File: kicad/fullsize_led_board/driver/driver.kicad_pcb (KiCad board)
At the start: 2 copper layers, 163.5 x 127.5 mm, 131 parts, among them J4 Anodes Header, J5 Cathodes Header, Q1 SQ2351CES, Q10 SQ2351CES, Q11 SQ2351CES, Q12 SQ2351CES, Q13 SQ2351CES, Q14 SQ2351CES, Q15 SQ2351CES, Q16 SQ2351CES, Q17 SQ2351CES, Q18 SQ2351CES, Q19 SQ2351CES, Q2 SQ2351CES, Q20 SQ2351CES, Q21 SQ2351CES, Q22 SQ2351CES, Q23 SQ2351CES, Q24 SQ2351CES, Q3 SQ2351CES, Q4 SQ2351CES, Q5 SQ2351CES, Q6 SQ2351CES, Q7 SQ2351CES, Q8 SQ2351CES, Q9 SQ2351CES, U1 74HCT541, U2 74HCT595, U3 74HCT595, U4 74HCT595, U5 TPIC6B595N, U6 TPIC6B595N, U7 TPIC6B595N, U8 TPIC6B595N

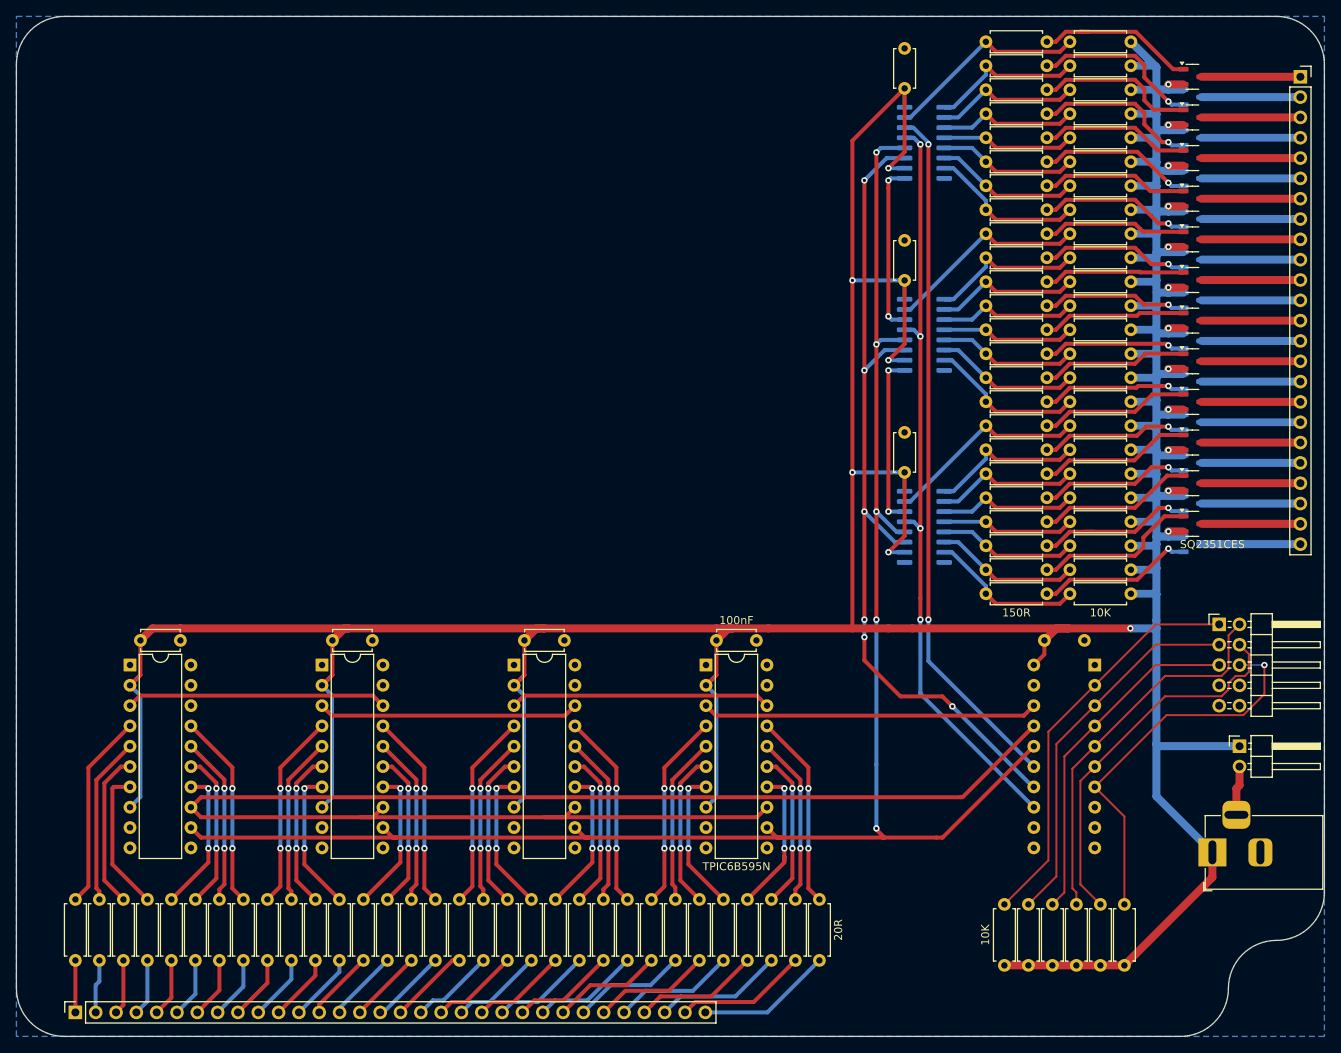
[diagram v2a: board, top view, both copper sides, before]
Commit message: fullsize led board: fixed backwards wiring
It's not as beautiful as I'd like to have it, but this will suffice, otherwise it will take way too much time to reroute the VIAs.
If I want to improve this design further, I'd like to use SMD resistors anyway, so a full rerout would be necessary.
Lesson learned I guess...
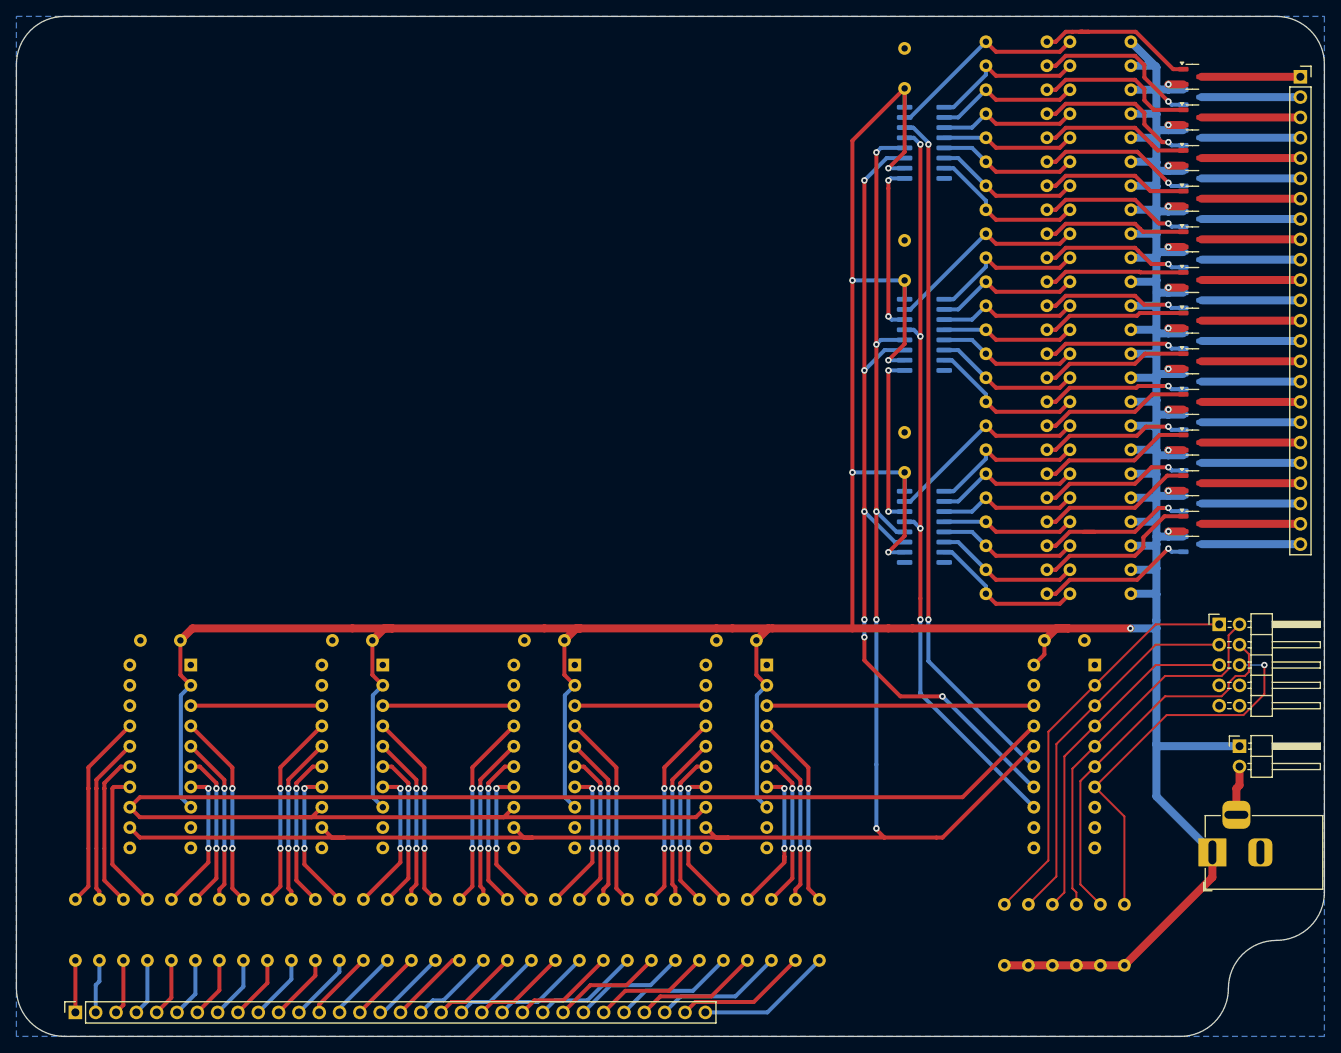
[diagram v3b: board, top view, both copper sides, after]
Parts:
- C2, C3, C4, C5, C6, C7, C8, R1, R10, R11, R12, R13, R14, R15, R16, R17, R18, R19, R2, R20, R21, R22, R23, R24, R25, R26, R27, R28, R29, R3, R30, R31, R32, R33, R34, R35, R36, R37, R38, R39, R4, R40, R41, R42, R43, R44, R45, R46, R47, R48, R49, R5, R50, R51, R52, R53, R54, R55, R56, R57, R58, R59, R6, R60, R61, R62, R63, R64, R65, R66, R67, R68, R69, R7, R70, R71, R72, R73, R74, R75, R76, R77, R78, R79, R8, R80, R81, R82, R83, R84, R85, R86, R9, U5, U6, U7, U8: moved to B.Cu
- moved R2 7.62 mm to (232.0, 143.5), turned to -90 degrees
- moved U6 7.60 mm to (142.3, 113.6), turned to 180 degrees
- moved U7 7.60 mm to (166.3, 113.6), turned to 180 degrees
- moved U8 7.60 mm to (190.3, 113.6), turned to 180 degrees
- moved U5 7.60 mm to (118.3, 113.6), turned to 180 degrees
- moved C5 5.00 mm to (117.0, 110.5), turned to 180 degrees
- moved C6 5.00 mm to (141.0, 110.5), turned to 180 degrees
- moved C7 5.00 mm to (165.0, 110.5), turned to 180 degrees
- moved C8 5.00 mm to (189.0, 110.5), turned to 180 degrees
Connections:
- R2 pad 1: +5V -> ShiftRowStrobe
- R2 pad 2: ShiftRowStrobe -> +5V
- U5 pad 14: /Cathodes4 -> /Cathodes3
- U5 pad 15: /Cathodes5 -> /Cathodes2
- U5 pad 16: /Cathodes6 -> /Cathodes1
- U5 pad 17: /Cathodes7 -> /Cathodes0
- U5 pad 4: /Cathodes0 -> /Cathodes7
- U5 pad 5: /Cathodes1 -> /Cathodes6
- U5 pad 6: /Cathodes2 -> /Cathodes5
- U5 pad 7: /Cathodes3 -> /Cathodes4
- U6 pad 14: /Cathodes12 -> /Cathodes11
- U6 pad 15: /Cathodes13 -> /Cathodes10
- U6 pad 16: /Cathodes14 -> /Cathodes9
- U6 pad 17: /Cathodes15 -> /Cathodes8
- U6 pad 4: /Cathodes8 -> /Cathodes15
- U6 pad 5: /Cathodes9 -> /Cathodes14
- U6 pad 6: /Cathodes10 -> /Cathodes13
- U6 pad 7: /Cathodes11 -> /Cathodes12
- U7 pad 14: /Cathodes20 -> /Cathodes19
- U7 pad 15: /Cathodes21 -> /Cathodes18
- U7 pad 16: /Cathodes22 -> /Cathodes17
- U7 pad 17: /Cathodes23 -> /Cathodes16
- U7 pad 4: /Cathodes16 -> /Cathodes23
- U7 pad 5: /Cathodes17 -> /Cathodes22
- U7 pad 6: /Cathodes18 -> /Cathodes21
- U7 pad 7: /Cathodes19 -> /Cathodes20
- U8 pad 14: /Cathodes28 -> /Cathodes27
- U8 pad 15: /Cathodes29 -> /Cathodes26
- U8 pad 16: /Cathodes30 -> /Cathodes25
- U8 pad 17: /Cathodes31 -> /Cathodes24
- U8 pad 4: /Cathodes24 -> /Cathodes31
- U8 pad 5: /Cathodes25 -> /Cathodes30
- U8 pad 6: /Cathodes26 -> /Cathodes29
- U8 pad 7: /Cathodes27 -> /Cathodes28
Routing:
- net Net-(U7-SER_IN): track 32.7 -> 16.4 mm
- net Net-(U6-SER_IN): track 32.7 -> 16.4 mm
- net Net-(U5-SER_IN): track 32.7 -> 16.4 mm
- net +5V: track 662.2 -> 649.3 mm
- net /ApplyRowAndStrobe': track 215.8 -> 225.9 mm
- net /RowData': track 42.0 -> 33.4 mm
- net /ShiftRowData': track 190.3 -> 198.1 mm

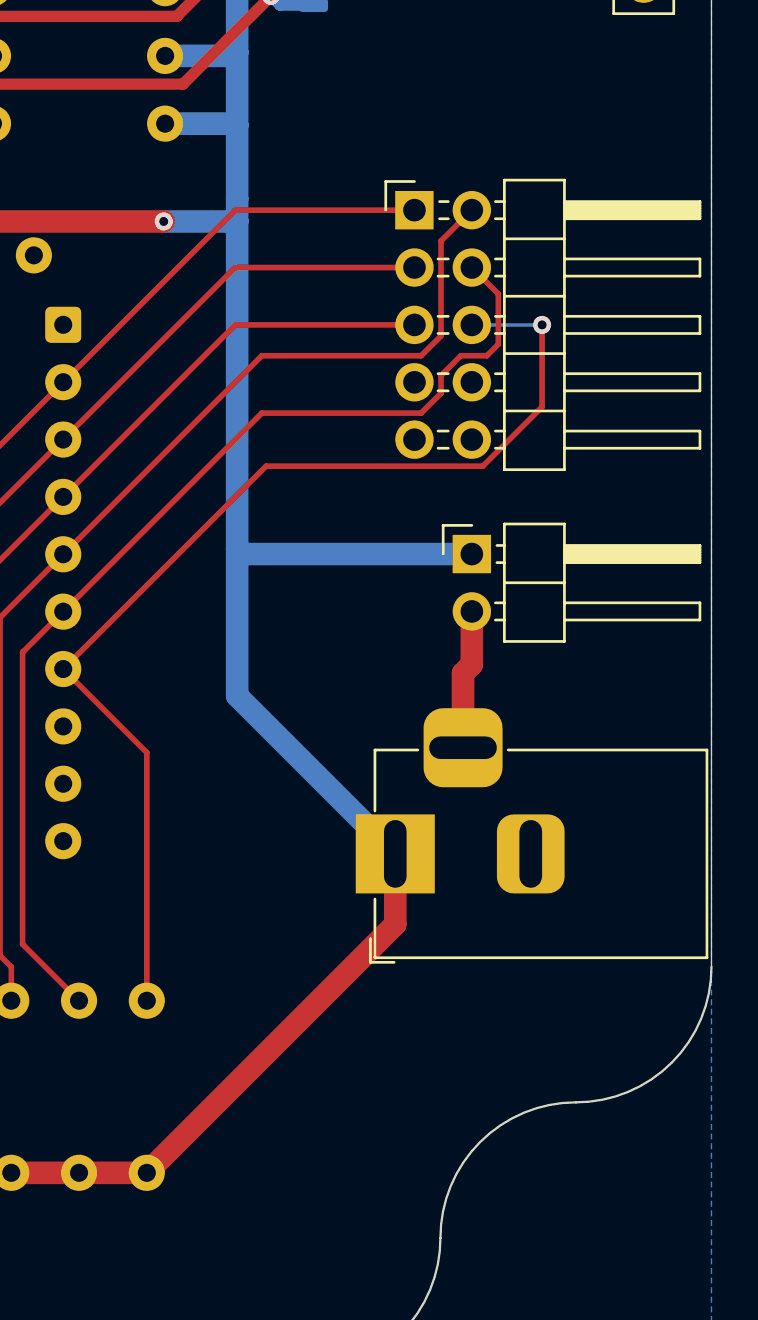
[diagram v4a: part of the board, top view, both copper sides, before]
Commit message: fullsize led board: moved pullups to +3.3v of pmod
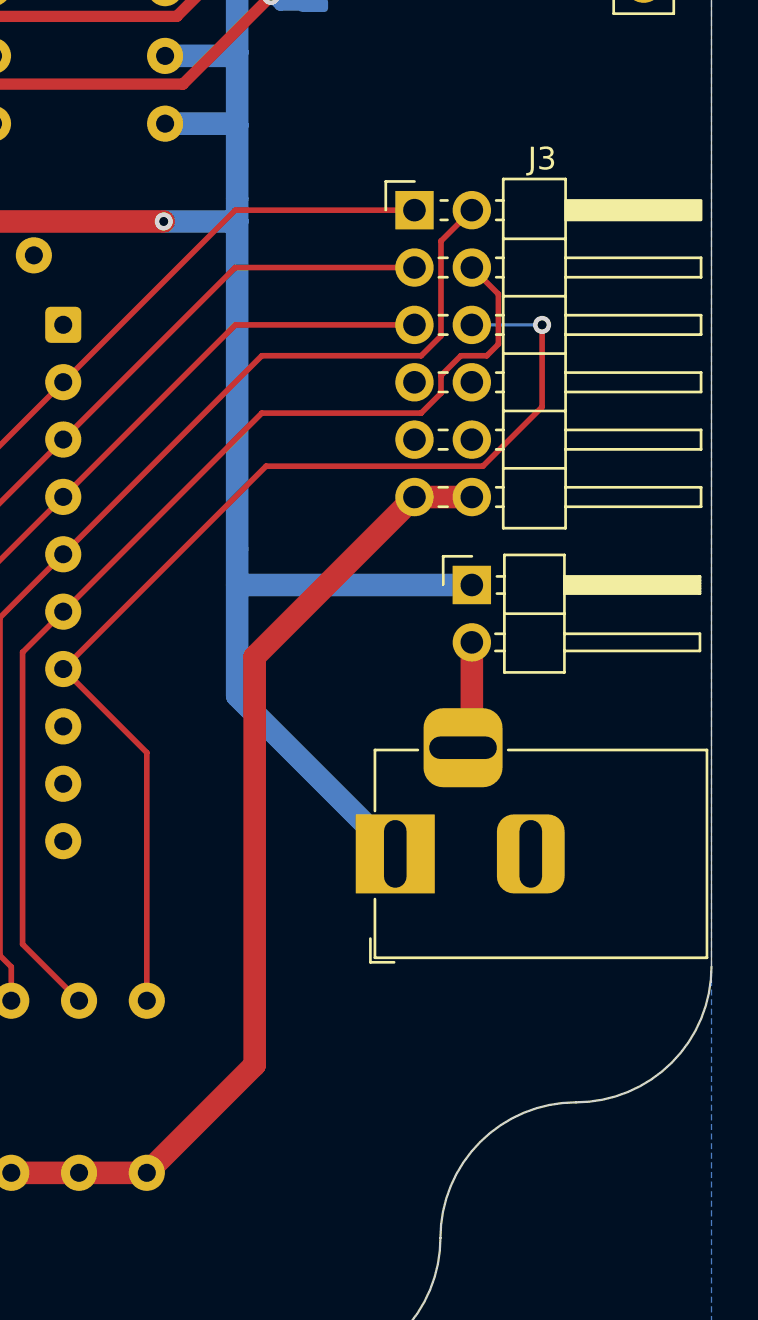
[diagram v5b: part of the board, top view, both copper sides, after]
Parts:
- J3: footprint Connector_PinHeader_2.54mm:PinHeader_2x05_P2.54mm_Horizontal -> Connector_PinHeader_2.54mm:PinHeader_2x06_P2.54mm_Horizontal
- moved J1 1.37 mm to (249.4, 125.1)
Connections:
- R1 pad 2: +5V -> 3.3V
- R2 pad 2: +5V -> 3.3V
- R3 pad 2: +5V -> 3.3V
- R4 pad 2: +5V -> 3.3V
- R5 pad 2: +5V -> 3.3V
- R6 pad 2: +5V -> 3.3V
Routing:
- net 3.3V: track 0.00 -> 52.4 mm
- net +5V: track 649.3 -> 615.5 mm
- net Net-(J1-Pin_2): track 6.20 -> 4.83 mm
